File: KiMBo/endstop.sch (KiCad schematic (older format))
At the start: 19 parts

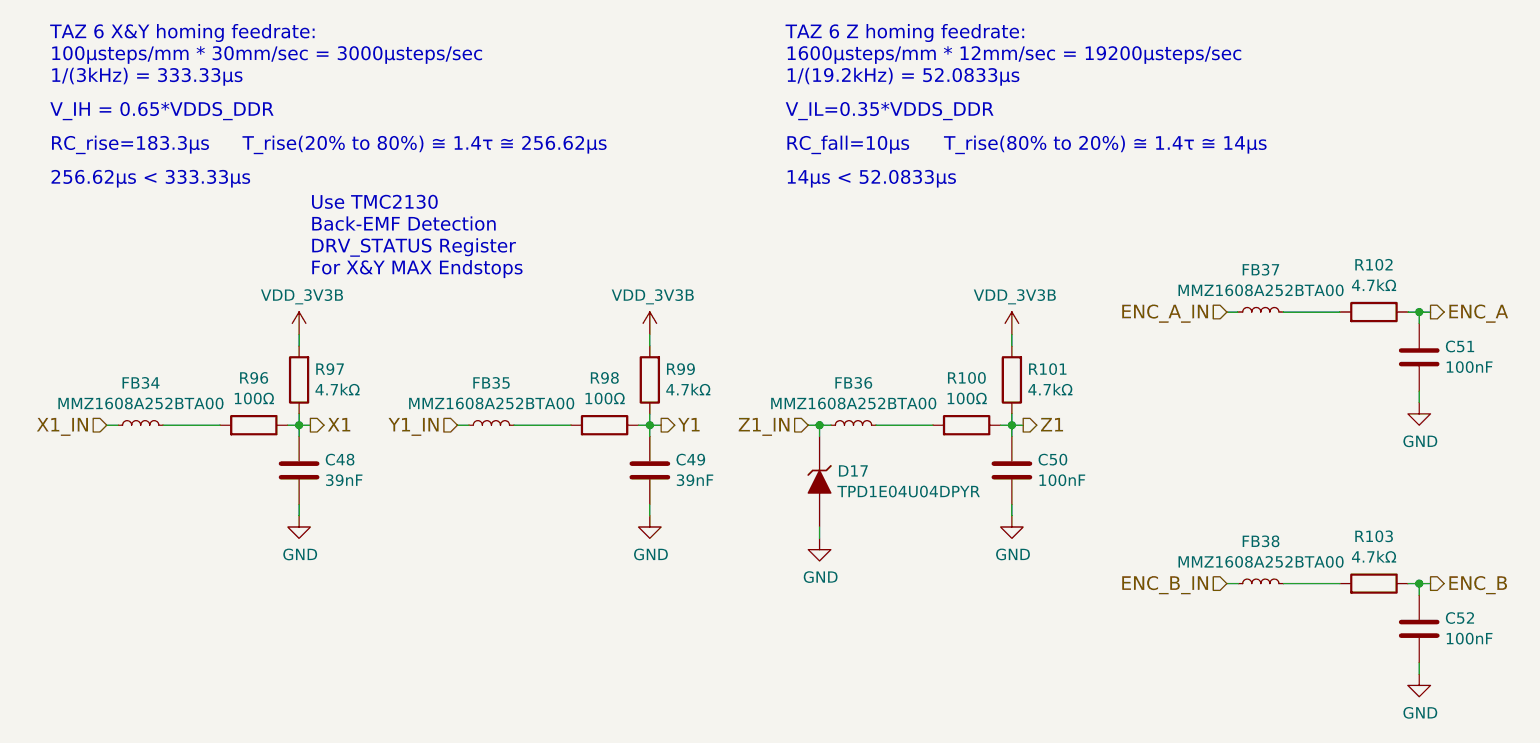
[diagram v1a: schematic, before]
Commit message: Route 24V to the buck, add PTC fuse to 5V output
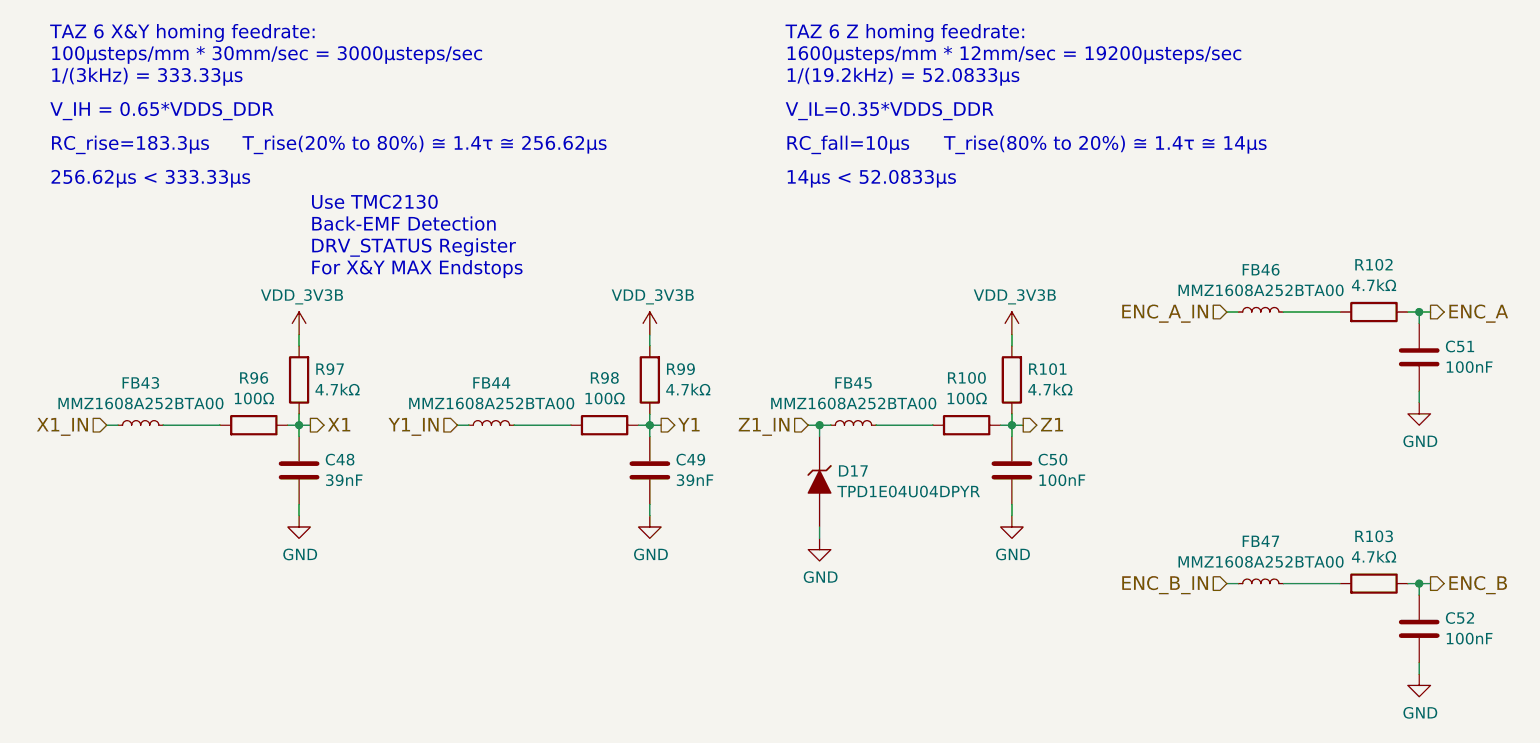
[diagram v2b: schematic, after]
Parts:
- renumbered FB34 to FB43, FB35 to FB44, FB36 to FB45, FB37 to FB46, FB38 to FB47
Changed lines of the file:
@@
 	7100 5300 7350 5300
 $Comp
-L INDUCTOR_Small FB34
+L INDUCTOR_Small FB43
 U 1 1 5B28F416
 P 5450 5300
-F 0 "FB34" V 5635 5300 50  0000 C CNN
+F 0 "FB43" V 5635 5300 50  0000 C CNN
 F 1 "MMZ1608A252BTA00" V 5544 5300 50  0000 C CNN
 F 2 "KiMBo:Ferrite_Bead_0603" H 5450 5300 50  0001 C CNN
@@
 	5550 5300 5800 5300
 $Comp
-L INDUCTOR_Small FB37
+L INDUCTOR_Small FB46
 U 1 1 5B292FBD
 P 10400 4800
-F 0 "FB37" V 10585 4800 50  0000 C CNN
+F 0 "FB46" V 10585 4800 50  0000 C CNN
 F 1 "MMZ1608A252BTA00" V 10494 4800 50  0000 C CNN
 F 2 "KiMBo:Ferrite_Bead_0603" H 10400 4800 50  0001 C CNN
@@
 $EndComp
 $Comp
-L INDUCTOR_Small FB38
+L INDUCTOR_Small FB47
 U 1 1 5B293036
 P 10400 6000
-F 0 "FB38" V 10585 6000 50  0000 C CNN
+F 0 "FB47" V 10585 6000 50  0000 C CNN
 F 1 "MMZ1608A252BTA00" V 10494 6000 50  0000 C CNN
 F 2 "KiMBo:Ferrite_Bead_0603" H 10400 6000 50  0001 C CNN
@@
 	8450 5800 8450 5750
 $Comp
-L INDUCTOR_Small FB35
+L INDUCTOR_Small FB44
 U 1 1 5B9752EE
 P 7000 5300
-F 0 "FB35" V 7185 5300 50  0000 C CNN
+F 0 "FB44" V 7185 5300 50  0000 C CNN
 F 1 "MMZ1608A252BTA00" V 7094 5300 50  0000 C CNN
 F 2 "KiMBo:Ferrite_Bead_0603" H 7000 5300 50  0001 C CNN
@@
 $EndComp
 $Comp
-L INDUCTOR_Small FB36
+L INDUCTOR_Small FB45
 U 1 1 5B975719
 P 8600 5300
-F 0 "FB36" V 8785 5300 50  0000 C CNN
+F 0 "FB45" V 8785 5300 50  0000 C CNN
 F 1 "MMZ1608A252BTA00" V 8694 5300 50  0000 C CNN
 F 2 "KiMBo:Ferrite_Bead_0603" H 8600 5300 50  0001 C CNN

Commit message: Add ferrite beads to the 5V and 3V pins at the SPI connectors
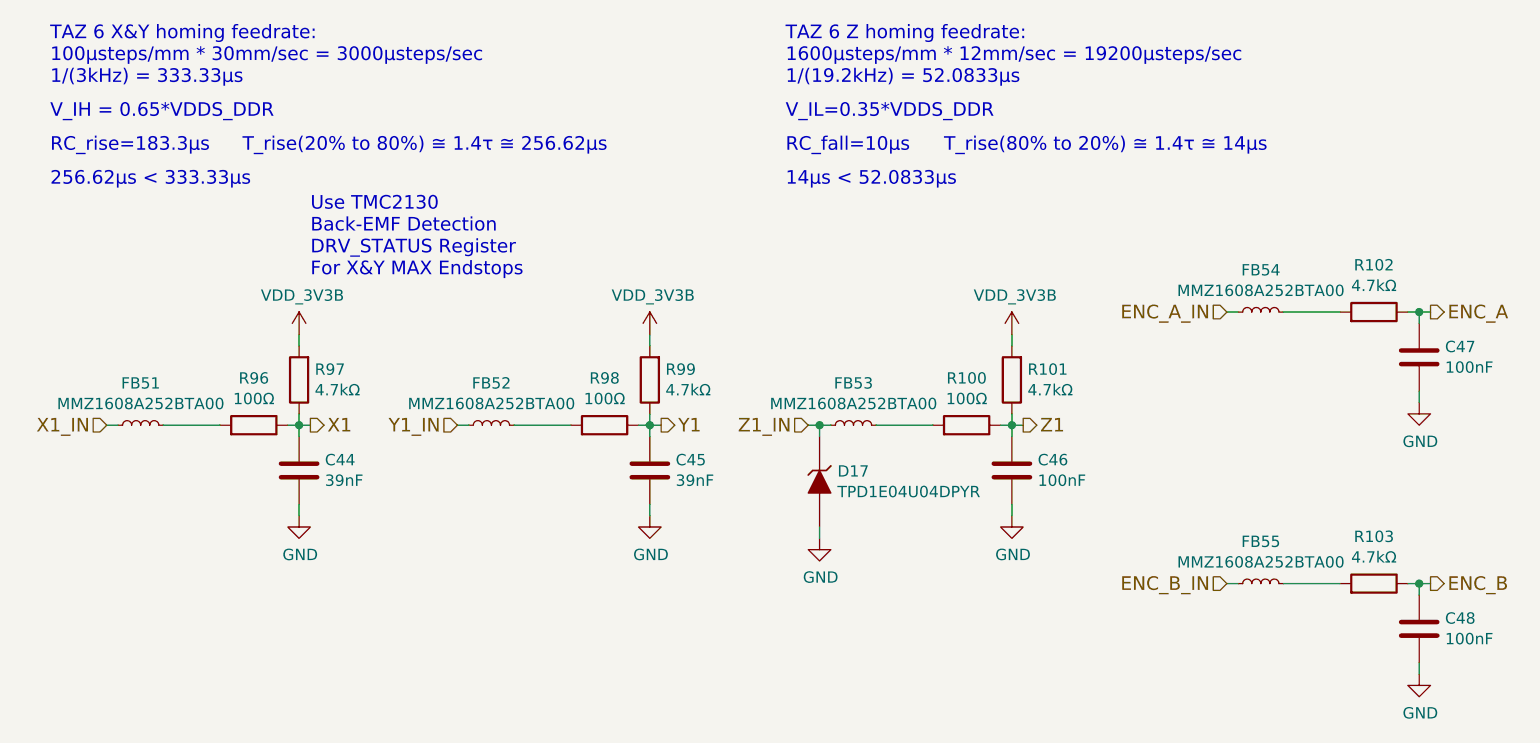
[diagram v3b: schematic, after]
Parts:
- renumbered C48 to C44, C49 to C45, C50 to C46, C51 to C47, C52 to C48, FB43 to FB51, FB44 to FB52, FB45 to FB53, FB46 to FB54, FB47 to FB55
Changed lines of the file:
@@
 X1
 $Comp
-L C C48
+L C C44
 U 1 1 58129032
 P 6150 5500
-F 0 "C48" H 6264 5546 50  0000 L CNN
+F 0 "C44" H 6264 5546 50  0000 L CNN
 F 1 "39nF" H 6264 5455 50  0000 L CNN
 F 2 "Capacitors_SMD:C_0603" H 6188 5350 50  0001 C CNN
@@
 Y1
 $Comp
-L C C49
+L C C45
 U 1 1 589415E7
 P 7700 5500
-F 0 "C49" H 7814 5546 50  0000 L CNN
+F 0 "C45" H 7814 5546 50  0000 L CNN
 F 1 "39nF" H 7814 5455 50  0000 L CNN
 F 2 "Capacitors_SMD:C_0603" H 7738 5350 50  0001 C CNN
@@
 Z1
 $Comp
-L C C50
+L C C46
 U 1 1 58941879
 P 9300 5500
-F 0 "C50" H 9414 5546 50  0000 L CNN
+F 0 "C46" H 9414 5546 50  0000 L CNN
 F 1 "100nF" H 9414 5455 50  0000 L CNN
 F 2 "Capacitors_SMD:C_0603" H 9338 5350 50  0001 C CNN
@@
 ENC_A
 $Comp
-L C C51
+L C C47
 U 1 1 5894C248
 P 11100 5000
-F 0 "C51" H 11214 5046 50  0000 L CNN
+F 0 "C47" H 11214 5046 50  0000 L CNN
 F 1 "100nF" H 11214 4955 50  0000 L CNN
 F 2 "Capacitors_SMD:C_0603" H 11138 4850 50  0001 C CNN
@@
 	11100 6000 11100 6050
 $Comp
-L C C52
+L C C48
 U 1 1 5894C2A4
 P 11100 6200
-F 0 "C52" H 11214 6246 50  0000 L CNN
+F 0 "C48" H 11214 6246 50  0000 L CNN
 F 1 "100nF" H 11214 6155 50  0000 L CNN
 F 2 "Capacitors_SMD:C_0603" H 11138 6050 50  0001 C CNN
@@
 ENC_B_IN
 $Comp
-L VDD_3V3B #PWR0146
+L VDD_3V3B #PWR0143
 U 1 1 59E67523
 P 6150 4900
-F 0 "#PWR0146" H 6150 4750 50  0001 C CNN
+F 0 "#PWR0143" H 6150 4750 50  0001 C CNN
 F 1 "VDD_3V3B" H 6165 5073 50  0000 C CNN
 F 2 "" H 6150 4900 50  0000 C CNN
@@
 $EndComp
 $Comp
-L VDD_3V3B #PWR0147
+L VDD_3V3B #PWR0144
 U 1 1 59E6755C
 P 7700 4900
-F 0 "#PWR0147" H 7700 4750 50  0001 C CNN
+F 0 "#PWR0144" H 7700 4750 50  0001 C CNN
 F 1 "VDD_3V3B" H 7715 5073 50  0000 C CNN
 F 2 "" H 7700 4900 50  0000 C CNN
@@
 $EndComp
 $Comp
-L VDD_3V3B #PWR0148
+L VDD_3V3B #PWR0145
 U 1 1 59E6758E
 P 9300 4900
-F 0 "#PWR0148" H 9300 4750 50  0001 C CNN
+F 0 "#PWR0145" H 9300 4750 50  0001 C CNN
 F 1 "VDD_3V3B" H 9315 5073 50  0000 C CNN
 F 2 "" H 9300 4900 50  0000 C CNN
@@
 	11050 6000 11150 6000
 $Comp
-L GND #PWR0149
+L GND #PWR0146
 U 1 1 59E68F88
 P 11100 5200
-F 0 "#PWR0149" H 11100 4950 50  0001 C CNN
+F 0 "#PWR0146" H 11100 4950 50  0001 C CNN
 F 1 "GND" H 11105 5027 50  0000 C CNN
 F 2 "" H 11100 5200 50  0000 C CNN
@@
 $EndComp
 $Comp
-L GND #PWR0150
+L GND #PWR0147
 U 1 1 59E68FBB
 P 11100 6400
-F 0 "#PWR0150" H 11100 6150 50  0001 C CNN
+F 0 "#PWR0147" H 11100 6150 50  0001 C CNN
 F 1 "GND" H 11105 6227 50  0000 C CNN
 F 2 "" H 11100 6400 50  0000 C CNN
@@
 $EndComp
 $Comp
-L GND #PWR0151
+L GND #PWR0148
 U 1 1 59E68FE7
 P 9300 5700
-F 0 "#PWR0151" H 9300 5450 50  0001 C CNN
+F 0 "#PWR0148" H 9300 5450 50  0001 C CNN
 F 1 "GND" H 9305 5527 50  0000 C CNN
 F 2 "" H 9300 5700 50  0000 C CNN
@@
 $EndComp
 $Comp
-L GND #PWR0152
+L GND #PWR0149
 U 1 1 59E69013
 P 7700 5700
-F 0 "#PWR0152" H 7700 5450 50  0001 C CNN
+F 0 "#PWR0149" H 7700 5450 50  0001 C CNN
 F 1 "GND" H 7705 5527 50  0000 C CNN
 F 2 "" H 7700 5700 50  0000 C CNN
@@
 $EndComp
 $Comp
-L GND #PWR0153
+L GND #PWR0150
 U 1 1 59E6903F
 P 6150 5700
-F 0 "#PWR0153" H 6150 5450 50  0001 C CNN
+F 0 "#PWR0150" H 6150 5450 50  0001 C CNN
 F 1 "GND" H 6155 5527 50  0000 C CNN
 F 2 "" H 6150 5700 50  0000 C CNN
@@
 	7100 5300 7350 5300
 $Comp
-L INDUCTOR_Small FB43
+L INDUCTOR_Small FB51
 U 1 1 5B28F416
 P 5450 5300
-F 0 "FB43" V 5635 5300 50  0000 C CNN
+F 0 "FB51" V 5635 5300 50  0000 C CNN
 F 1 "MMZ1608A252BTA00" V 5544 5300 50  0000 C CNN
 F 2 "KiMBo:Ferrite_Bead_0603" H 5450 5300 50  0001 C CNN
@@
 	5550 5300 5800 5300
 $Comp
-L INDUCTOR_Small FB46
+L INDUCTOR_Small FB54
 U 1 1 5B292FBD
 P 10400 4800
-F 0 "FB46" V 10585 4800 50  0000 C CNN
+F 0 "FB54" V 10585 4800 50  0000 C CNN
 F 1 "MMZ1608A252BTA00" V 10494 4800 50  0000 C CNN
 F 2 "KiMBo:Ferrite_Bead_0603" H 10400 4800 50  0001 C CNN
@@
 $EndComp
 $Comp
-L INDUCTOR_Small FB47
+L INDUCTOR_Small FB55
 U 1 1 5B293036
 P 10400 6000
-F 0 "FB47" V 10585 6000 50  0000 C CNN
+F 0 "FB55" V 10585 6000 50  0000 C CNN
 F 1 "MMZ1608A252BTA00" V 10494 6000 50  0000 C CNN
 F 2 "KiMBo:Ferrite_Bead_0603" H 10400 6000 50  0001 C CNN
@@
 Connection ~ 8450 5300
 $Comp
-L GND #PWR0154
+L GND #PWR0151
 U 1 1 5B4EDFC5
 P 8450 5800
-F 0 "#PWR0154" H 8450 5550 50  0001 C CNN
+F 0 "#PWR0151" H 8450 5550 50  0001 C CNN
 F 1 "GND" H 8455 5627 50  0000 C CNN
 F 2 "" H 8450 5800 50  0000 C CNN
@@
 	8450 5800 8450 5750
 $Comp
-L INDUCTOR_Small FB44
+L INDUCTOR_Small FB52
 U 1 1 5B9752EE
 P 7000 5300
-F 0 "FB44" V 7185 5300 50  0000 C CNN
+F 0 "FB52" V 7185 5300 50  0000 C CNN
 F 1 "MMZ1608A252BTA00" V 7094 5300 50  0000 C CNN
 F 2 "KiMBo:Ferrite_Bead_0603" H 7000 5300 50  0001 C CNN
@@
 $EndComp
 $Comp
-L INDUCTOR_Small FB45
+L INDUCTOR_Small FB53
 U 1 1 5B975719
 P 8600 5300
-F 0 "FB45" V 8785 5300 50  0000 C CNN
+F 0 "FB53" V 8785 5300 50  0000 C CNN
 F 1 "MMZ1608A252BTA00" V 8694 5300 50  0000 C CNN
 F 2 "KiMBo:Ferrite_Bead_0603" H 8600 5300 50  0001 C CNN

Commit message: Complete SPI, ADC, and Endstop header layout/position, add zone around the SiP
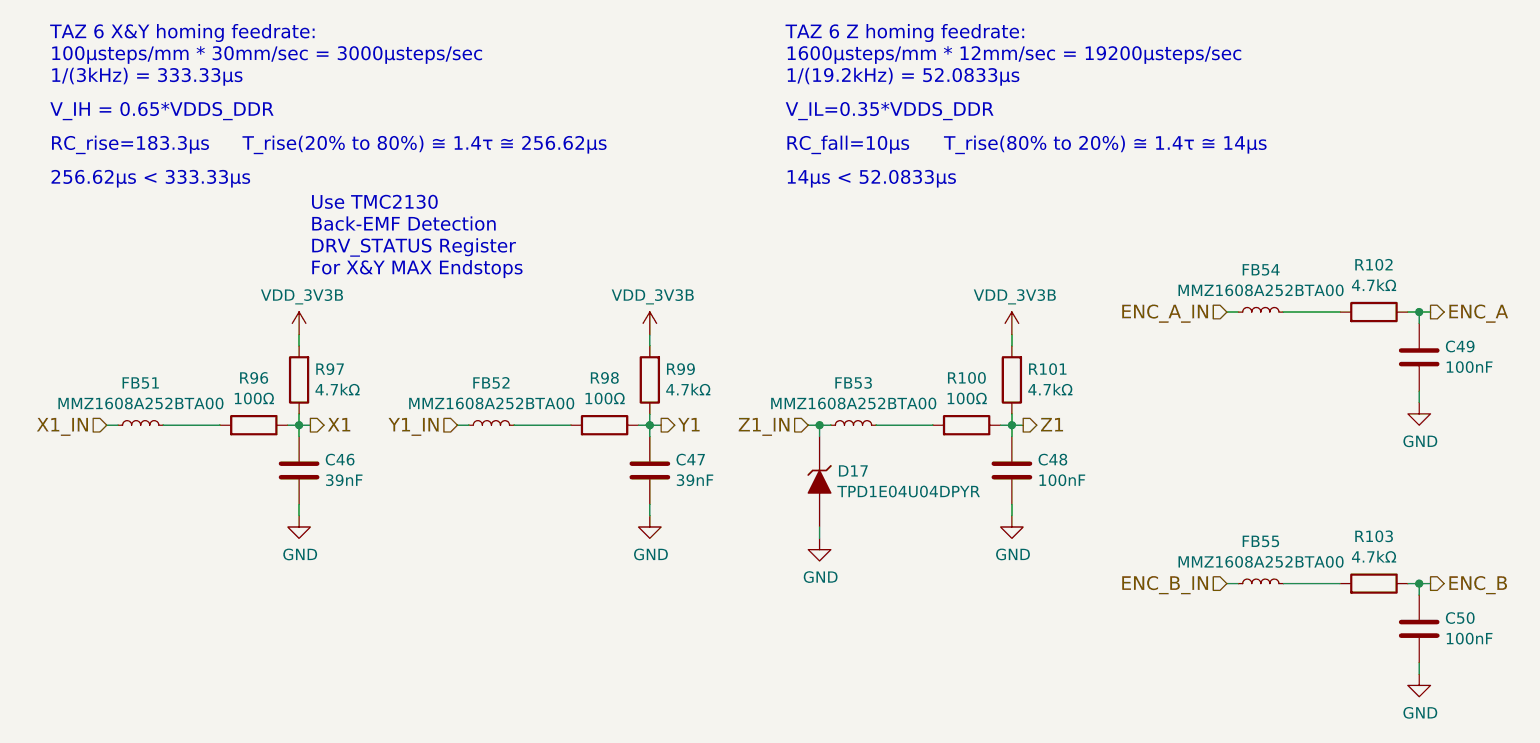
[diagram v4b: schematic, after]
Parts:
- renumbered C44 to C46, C45 to C47, C46 to C48, C47 to C49, C48 to C50
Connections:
- net ENC_A_IN: now also FB54.2; no longer FB54.1
- net ENC_B_IN: now also FB55.2; no longer FB55.1
- net X1_IN: now also FB51.2; no longer FB51.1
- net Y1_IN: now also FB52.2; no longer FB52.1
- net Z1_IN: now also FB53.2; no longer FB53.1
- net at R96.2: now also FB51.1; no longer FB51.2
- net at R98.2: now also FB52.1; no longer FB52.2
- net at R100.2: now also FB53.1; no longer FB53.2
- net at R102.2: now also FB54.1; no longer FB54.2
- net at R103.2: now also FB55.1; no longer FB55.2
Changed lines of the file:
@@
 X1
 $Comp
-L C C44
+L C C46
 U 1 1 58129032
 P 6150 5500
-F 0 "C44" H 6264 5546 50  0000 L CNN
+F 0 "C46" H 6264 5546 50  0000 L CNN
 F 1 "39nF" H 6264 5455 50  0000 L CNN
 F 2 "Capacitors_SMD:C_0603" H 6188 5350 50  0001 C CNN
@@
 Y1
 $Comp
-L C C45
+L C C47
 U 1 1 589415E7
 P 7700 5500
-F 0 "C45" H 7814 5546 50  0000 L CNN
+F 0 "C47" H 7814 5546 50  0000 L CNN
 F 1 "39nF" H 7814 5455 50  0000 L CNN
 F 2 "Capacitors_SMD:C_0603" H 7738 5350 50  0001 C CNN
@@
 Z1
 $Comp
-L C C46
+L C C48
 U 1 1 58941879
 P 9300 5500
-F 0 "C46" H 9414 5546 50  0000 L CNN
+F 0 "C48" H 9414 5546 50  0000 L CNN
 F 1 "100nF" H 9414 5455 50  0000 L CNN
 F 2 "Capacitors_SMD:C_0603" H 9338 5350 50  0001 C CNN
@@
 ENC_A
 $Comp
-L C C47
+L C C49
 U 1 1 5894C248
 P 11100 5000
-F 0 "C47" H 11214 5046 50  0000 L CNN
+F 0 "C49" H 11214 5046 50  0000 L CNN
 F 1 "100nF" H 11214 4955 50  0000 L CNN
 F 2 "Capacitors_SMD:C_0603" H 11138 4850 50  0001 C CNN
@@
 	11100 6000 11100 6050
 $Comp
-L C C48
+L C C50
 U 1 1 5894C2A4
 P 11100 6200
-F 0 "C48" H 11214 6246 50  0000 L CNN
+F 0 "C50" H 11214 6246 50  0000 L CNN
 F 1 "100nF" H 11214 6155 50  0000 L CNN
 F 2 "Capacitors_SMD:C_0603" H 11138 6050 50  0001 C CNN
@@
 ENC_B_IN
 $Comp
-L VDD_3V3B #PWR0143
+L VDD_3V3B #PWR0145
 U 1 1 59E67523
 P 6150 4900
-F 0 "#PWR0143" H 6150 4750 50  0001 C CNN
+F 0 "#PWR0145" H 6150 4750 50  0001 C CNN
 F 1 "VDD_3V3B" H 6165 5073 50  0000 C CNN
 F 2 "" H 6150 4900 50  0000 C CNN
@@
 $EndComp
 $Comp
-L VDD_3V3B #PWR0144
+L VDD_3V3B #PWR0146
 U 1 1 59E6755C
 P 7700 4900
-F 0 "#PWR0144" H 7700 4750 50  0001 C CNN
+F 0 "#PWR0146" H 7700 4750 50  0001 C CNN
 F 1 "VDD_3V3B" H 7715 5073 50  0000 C CNN
 F 2 "" H 7700 4900 50  0000 C CNN
@@
 $EndComp
 $Comp
-L VDD_3V3B #PWR0145
+L VDD_3V3B #PWR0147
 U 1 1 59E6758E
 P 9300 4900
-F 0 "#PWR0145" H 9300 4750 50  0001 C CNN
+F 0 "#PWR0147" H 9300 4750 50  0001 C CNN
 F 1 "VDD_3V3B" H 9315 5073 50  0000 C CNN
 F 2 "" H 9300 4900 50  0000 C CNN
@@
 	11050 6000 11150 6000
 $Comp
-L GND #PWR0146
+L GND #PWR0148
 U 1 1 59E68F88
 P 11100 5200
-F 0 "#PWR0146" H 11100 4950 50  0001 C CNN
+F 0 "#PWR0148" H 11100 4950 50  0001 C CNN
 F 1 "GND" H 11105 5027 50  0000 C CNN
 F 2 "" H 11100 5200 50  0000 C CNN
@@
 $EndComp
 $Comp
-L GND #PWR0147
+L GND #PWR0149
 U 1 1 59E68FBB
 P 11100 6400
-F 0 "#PWR0147" H 11100 6150 50  0001 C CNN
+F 0 "#PWR0149" H 11100 6150 50  0001 C CNN
 F 1 "GND" H 11105 6227 50  0000 C CNN
 F 2 "" H 11100 6400 50  0000 C CNN
@@
 $EndComp
 $Comp
-L GND #PWR0148
+L GND #PWR0150
 U 1 1 59E68FE7
 P 9300 5700
-F 0 "#PWR0148" H 9300 5450 50  0001 C CNN
+F 0 "#PWR0150" H 9300 5450 50  0001 C CNN
 F 1 "GND" H 9305 5527 50  0000 C CNN
 F 2 "" H 9300 5700 50  0000 C CNN
@@
 $EndComp
 $Comp
-L GND #PWR0149
+L GND #PWR0151
 U 1 1 59E69013
 P 7700 5700
-F 0 "#PWR0149" H 7700 5450 50  0001 C CNN
+F 0 "#PWR0151" H 7700 5450 50  0001 C CNN
 F 1 "GND" H 7705 5527 50  0000 C CNN
 F 2 "" H 7700 5700 50  0000 C CNN
@@
 $EndComp
 $Comp
-L GND #PWR0150
+L GND #PWR0152
 U 1 1 59E6903F
 P 6150 5700
-F 0 "#PWR0150" H 6150 5450 50  0001 C CNN
+F 0 "#PWR0152" H 6150 5450 50  0001 C CNN
 F 1 "GND" H 6155 5527 50  0000 C CNN
 F 2 "" H 6150 5700 50  0000 C CNN
@@
 F 3 "" H 5450 5300 50  0000 C CNN
 	1    5450 5300
-	0    -1   -1   0
+	0    1    -1   0
 $EndComp
 Wire Wire Line
@@
 F 3 "" H 10400 4800 50  0000 C CNN
 	1    10400 4800
-	0    -1   -1   0
+	0    1    -1   0
 $EndComp
 $Comp
@@
 F 3 "" H 10400 6000 50  0000 C CNN
 	1    10400 6000
-	0    -1   -1   0
+	0    1    -1   0
 $EndComp
 Wire Wire Line
@@
 Connection ~ 8450 5300
 $Comp
-L GND #PWR0151
+L GND #PWR0153
 U 1 1 5B4EDFC5
 P 8450 5800
-F 0 "#PWR0151" H 8450 5550 50  0001 C CNN
+F 0 "#PWR0153" H 8450 5550 50  0001 C CNN
 F 1 "GND" H 8455 5627 50  0000 C CNN
 F 2 "" H 8450 5800 50  0000 C CNN
@@
 F 3 "" H 7000 5300 50  0000 C CNN
 	1    7000 5300
-	0    -1   -1   0
+	0    1    -1   0
 $EndComp
 $Comp
@@
 F 3 "" H 8600 5300 50  0000 C CNN
 	1    8600 5300
-	0    -1   -1   0
+	0    1    -1   0
 $EndComp
 Text Notes 8300 4100 0    60   ~ 0
